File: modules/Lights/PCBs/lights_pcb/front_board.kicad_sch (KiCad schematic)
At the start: 6 parts, among them J1 THONKICONN, J2 THONKICONN, J3 THONKICONN, J4 THONKICONN, SW1 TL1105SPF250Q

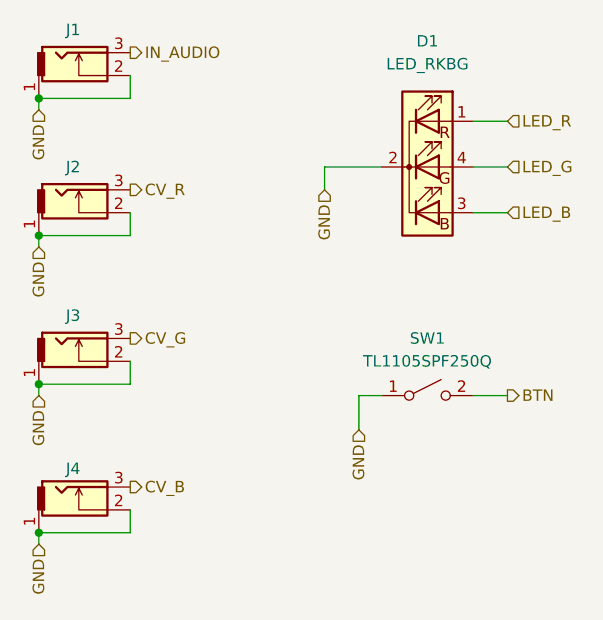
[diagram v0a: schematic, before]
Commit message: Switch lights to external 3.3V power supply instead of using rpi pico
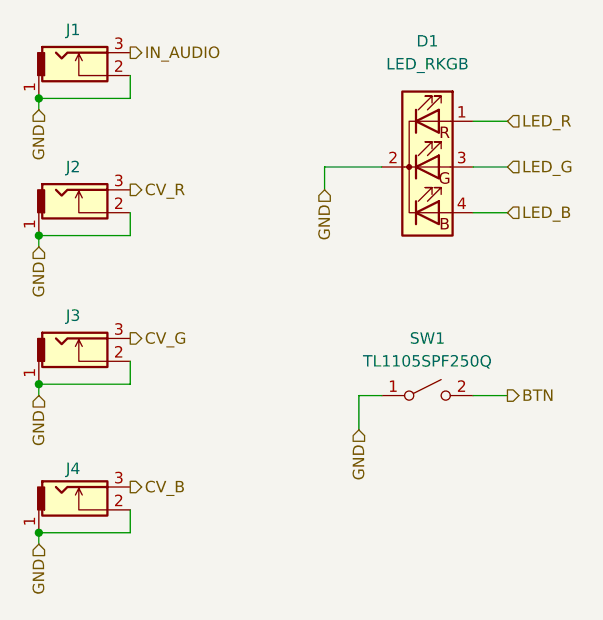
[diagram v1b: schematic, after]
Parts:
- removed D1: LED_RKBG, LED_THT:LED_D5.0mm-4_RGB, symbol Device:LED_RKBG
- added D1: LED_RKGB, LED_THT:LED_D5.0mm-4_RGB, symbol Device:LED_RKGB
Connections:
- net GND: now also D1.2 (K)
- net LED_B: now also D1.4 (BA)
- net LED_G: now also D1.3 (GA)
- net LED_R: now also D1.1 (RA)
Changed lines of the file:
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@@
 	)
 	(symbol
-		(lib_id "Device:LED_RKBG")
+		(lib_id "FreeModular:THONKICONN")
+		(at 68.58 76.2 0)
+		(unit 1)
+		(exclude_from_sim no)
+		(in_bom yes)
+		(on_board yes)
+		(dnp no)
+		(fields_autoplaced yes)
+		(property "Reference" "J2"
+			(at 67.31 71.12 0)
+			(effects
+				(font
+					(size 1.27 1.27)
+				)
+			)
+		)
+		(property "Value" "THONKICONN"
+			(at 69.85 78.74 0)
+			(effects
+				(font
+					(size 1.27 1.27)
+				)
+				(hide yes)
+			)
+		)
+		(property "Footprint" "FreeModular:THONKICONN"
+			(at 74.93 73.66 0)
+			(effects
+				(font
+					(size 1.27 1.27)
+				)
+				(hide yes)
+			)
+		)
+		(property "Datasheet" "~"
+			(at 74.93 73.66 0)
+			(effects
+				(font
+					(size 1.27 1.27)
+				)
+				(hide yes)
+			)
+		)
+		(property "Description" "2-pin audio jack receptable (mono/TS connector) with switching contact"
+			(at 68.58 76.2 0)
+			(effects
+				(font
+					(size 1.27 1.27)
+				)
+				(hide yes)
+			)
+		)
+		(pin "2"
+		)
+		(pin "3"
+		)
+		(pin "1"
+		)
+		(instances
+			(project "lights_pcb"
+				(path "/bf0b830d-6ea8-4ffe-b350-63f7ac69529d/657d6a20-99d4-49b9-af36-5ff58c444039"
+					(reference "J2")
+					(unit 1)
+				)
+			)
+		)
+	)
+	(symbol
+		(lib_id "FreeModular:THONKICONN")
+		(at 68.58 109.22 0)
+		(unit 1)
+		(exclude_from_sim no)
+		(in_bom yes)
+		(on_board yes)
+		(dnp no)
+		(property "Reference" "J4"
+			(at 67.31 104.648 0)
+			(effects
+				(font
+					(size 1.27 1.27)
+				)
+			)
+		)
+		(property "Value" "THONKICONN"
+			(at 69.85 111.76 0)
+			(effects
+				(font
+					(size 1.27 1.27)
+				)
+				(hide yes)
+			)
+		)
+		(property "Footprint" "FreeModular:THONKICONN"
+			(at 74.93 106.68 0)
+			(effects
+				(font
+					(size 1.27 1.27)
+				)
+				(hide yes)
+			)
+		)
+		(property "Datasheet" "~"
+			(at 74.93 106.68 0)
+			(effects
+				(font
+					(size 1.27 1.27)
+				)
+				(hide yes)
+			)
+		)
+		(property "Description" "2-pin audio jack receptable (mono/TS connector) with switching contact"
+			(at 68.58 109.22 0)
+			(effects
+				(font
+					(size 1.27 1.27)
+				)
+				(hide yes)
+			)
+		)
+		(pin "2"
+		)
+		(pin "3"
+		)
+		(pin "1"
+		)
+		(instances
+			(project "lights_pcb"
+				(path "/bf0b830d-6ea8-4ffe-b350-63f7ac69529d/657d6a20-99d4-49b9-af36-5ff58c444039"
+					(reference "J4")
+					(unit 1)
+				)
+			)
+		)
+	)
+	(symbol
+		(lib_id "FreeModular:THONKICONN")
+		(at 68.58 60.96 0)
+		(unit 1)
+		(exclude_from_sim no)
+		(in_bom yes)
+		(on_board yes)
+		(dnp no)
+		(fields_autoplaced yes)
+		(property "Reference" "J1"
+			(at 67.31 55.88 0)
+			(effects
+				(font
+					(size 1.27 1.27)
+				)
+			)
+		)
+		(property "Value" "THONKICONN"
+			(at 69.85 63.5 0)
+			(effects
+				(font
+					(size 1.27 1.27)
+				)
+				(hide yes)
+			)
+		)
+		(property "Footprint" "FreeModular:THONKICONN"
+			(at 74.93 58.42 0)
+			(effects
+				(font
+					(size 1.27 1.27)
+				)
+				(hide yes)
+			)
+		)
+		(property "Datasheet" "~"
+			(at 74.93 58.42 0)
+			(effects
+				(font
+					(size 1.27 1.27)
+				)
+				(hide yes)
+			)
+		)
+		(property "Description" "2-pin audio jack receptable (mono/TS connector) with switching contact"
+			(at 68.58 60.96 0)
+			(effects
+				(font
+					(size 1.27 1.27)
+				)
+				(hide yes)
+			)
+		)
+		(pin "2"
+		)
+		(pin "3"
+		)
+		(pin "1"
+		)
+		(instances
+			(project "lights_pcb"
+				(path "/bf0b830d-6ea8-4ffe-b350-63f7ac69529d/657d6a20-99d4-49b9-af36-5ff58c444039"
+					(reference "J1")
+					(unit 1)
+				)
+			)
+		)
+	)
+	(symbol
+		(lib_id "Device:LED_RKGB")
 		(at 106.68 71.12 0)
 		(unit 1)
@@
 			)
 		)
-		(property "Value" "LED_RKBG"
+		(property "Value" "LED_RKGB"
 			(at 106.68 59.69 0)
 			(effects
@@
 			)
 		)
-		(property "Description" "RGB LED, red/cathode/blue/green"
+		(property "Description" "RGB LED, red/cathode/green/blue"
 			(at 106.68 71.12 0)
 			(effects
@@
 		(pin "1"
 		)
+		(pin "2"
+		)
 		(pin "4"
 		)
-		(pin "2"
-		)
 		(instances
 			(project ""
@@
 					(unit 1)
 				)
-			)
-		)
-	)
-	(symbol
-		(lib_id "FreeModular:THONKICONN")
-		(at 68.58 76.2 0)
-		(unit 1)
-		(exclude_from_sim no)
-		(in_bom yes)
-		(on_board yes)
-		(dnp no)
-		(fields_autoplaced yes)
-		(property "Reference" "J2"
-			(at 67.31 71.12 0)
-			(effects
-				(font
-					(size 1.27 1.27)
-				)
-			)
-		)
-		(property "Value" "THONKICONN"
-			(at 69.85 78.74 0)
-			(effects
-				(font
-					(size 1.27 1.27)
-				)
-				(hide yes)
-			)
-		)
-		(property "Footprint" "FreeModular:THONKICONN"
-			(at 74.93 73.66 0)
-			(effects
-				(font
-					(size 1.27 1.27)
-				)
-				(hide yes)
-			)
-		)
-		(property "Datasheet" "~"
-			(at 74.93 73.66 0)
-			(effects
-				(font
-					(size 1.27 1.27)
-				)
-				(hide yes)
-			)
-		)
-		(property "Description" "2-pin audio jack receptable (mono/TS connector) with switching contact"
-			(at 68.58 76.2 0)
-			(effects
-				(font
-					(size 1.27 1.27)
-				)
-				(hide yes)
-			)
-		)
-		(pin "2"
-		)
-		(pin "3"
-		)
-		(pin "1"
-		)
-		(instances
-			(project "lights_pcb"
-				(path "/bf0b830d-6ea8-4ffe-b350-63f7ac69529d/657d6a20-99d4-49b9-af36-5ff58c444039"
-					(reference "J2")
-					(unit 1)
-				)
-			)
-		)
-	)
-	(symbol
-		(lib_id "FreeModular:THONKICONN")
-		(at 68.58 109.22 0)
-		(unit 1)
-		(exclude_from_sim no)
-		(in_bom yes)
-		(on_board yes)
-		(dnp no)
-		(property "Reference" "J4"
-			(at 67.31 104.648 0)
-			(effects
-				(font
-					(size 1.27 1.27)
-				)
-			)
-		)
-		(property "Value" "THONKICONN"
-			(at 69.85 111.76 0)
-			(effects
-				(font
-					(size 1.27 1.27)
-				)
-				(hide yes)
-			)
-		)
-		(property "Footprint" "FreeModular:THONKICONN"
-			(at 74.93 106.68 0)
-			(effects
-				(font
-					(size 1.27 1.27)
-				)
-				(hide yes)
-			)
-		)
-		(property "Datasheet" "~"
-			(at 74.93 106.68 0)
-			(effects
-				(font
-					(size 1.27 1.27)
-				)
-				(hide yes)
-			)
-		)
-		(property "Description" "2-pin audio jack receptable (mono/TS connector) with switching contact"
-			(at 68.58 109.22 0)
-			(effects
-				(font
-					(size 1.27 1.27)
-				)
-				(hide yes)
-			)
-		)
-		(pin "2"
-		)
-		(pin "3"
-		)
-		(pin "1"
-		)
-		(instances
-			(project "lights_pcb"
-				(path "/bf0b830d-6ea8-4ffe-b350-63f7ac69529d/657d6a20-99d4-49b9-af36-5ff58c444039"
-					(reference "J4")
-					(unit 1)
-				)
-			)
-		)
-	)
-	(symbol
-		(lib_id "FreeModular:THONKICONN")
-		(at 68.58 60.96 0)
-		(unit 1)
-		(exclude_from_sim no)
-		(in_bom yes)
-		(on_board yes)
-		(dnp no)
-		(fields_autoplaced yes)
-		(property "Reference" "J1"
-			(at 67.31 55.88 0)
-			(effects
-				(font
-					(size 1.27 1.27)
-				)
-			)
-		)
-		(property "Value" "THONKICONN"
-			(at 69.85 63.5 0)
-			(effects
-				(font
-					(size 1.27 1.27)
-				)
-				(hide yes)
-			)
-		)
-		(property "Footprint" "FreeModular:THONKICONN"
-			(at 74.93 58.42 0)
-			(effects
-				(font
-					(size 1.27 1.27)
-				)
-				(hide yes)
-			)
-		)
-		(property "Datasheet" "~"
-			(at 74.93 58.42 0)
-			(effects
-				(font
-					(size 1.27 1.27)
-				)
-				(hide yes)
-			)
-		)
-		(property "Description" "2-pin audio jack receptable (mono/TS connector) with switching contact"
-			(at 68.58 60.96 0)
-			(effects
-				(font
-					(size 1.27 1.27)
-				)
-				(hide yes)
-			)
-		)
-		(pin "2"
-		)
-		(pin "3"
-		)
-		(pin "1"
-		)
-		(instances
-			(project "lights_pcb"
-				(path "/bf0b830d-6ea8-4ffe-b350-63f7ac69529d/657d6a20-99d4-49b9-af36-5ff58c444039"
-					(reference "J1")
-					(unit 1)
-				)
